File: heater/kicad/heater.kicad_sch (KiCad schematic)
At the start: 85 parts, among them J1 Conn_01x02_Pin, J2 Conn_01x02_Pin, J3 pcie_98, U1 OPA863SIDBVR, U11 ESD5344D-TP, U12 ESD5344D-TP, U13 XC6206P332MR, U15 TPS7A2025PDBVR, U2 D050505T-1WR4, U3 LTC1966, U5 TPS72325DBVR, U6 LTC1966, U8 ADS1115IDGS, U9 ISO1541

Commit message: Updated heater shecmatic and sys config.
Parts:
- R6: value 10K -> 1K; LCSC C25744 -> C11702
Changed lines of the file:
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@@
       (effects (font (size 1.27 1.27)))
     )
-    (property "Value" "10K" (at 138.43 123.19 90)
+    (property "Value" "1K" (at 138.43 123.19 90)
       (effects (font (size 1.27 1.27)))
     )
@@
       (effects (font (size 1.27 1.27)) hide)
     )
-    (property "LCSC" "C25744" (at 138.43 125.73 0)
+    (property "LCSC" "C11702" (at 138.43 125.73 0)
       (effects (font (size 1.27 1.27)) hide)
     )

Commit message: Changed value of isense op amp serial resistor.
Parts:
- R6: value 1K -> 910R; LCSC C11702 -> (none)
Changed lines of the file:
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@@
       (effects (font (size 1.27 1.27)))
     )
-    (property "Value" "1K" (at 138.43 123.19 90)
+    (property "Value" "910R" (at 138.43 123.19 90)
       (effects (font (size 1.27 1.27)))
     )
@@
       (effects (font (size 1.27 1.27)) hide)
     )
-    (property "LCSC" "C11702" (at 138.43 125.73 0)
+    (property "LCSC" "" (at 138.43 125.73 0)
       (effects (font (size 1.27 1.27)) hide)
     )

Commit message: Fixed the heater schematic title.
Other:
- title: ADS1261B ADC BOARD -> PWM Power Measurement Card.
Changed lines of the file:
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@@
   (paper "User" 381 279.4)
   (title_block
-    (title "ADS1261B ADC BOARD")
+    (title "PWM Power Measurement Card.")
     (rev "0.2")
   )

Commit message: Changed the I sense op amp to a low bias current one.
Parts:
- R6: value 910R -> 10K; LCSC (none) -> C25744
- U1: value OPA863SIDBVR -> OPA810IDBV; LCSC C4369756 -> C2833513
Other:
- note added: "NOTES: * LCSC part number are of approximated values to maximize usage of JLCPCB 'basic' parts. * Accuracy can be improved by suing low ppm resistors where applicable and a film capacitor for the RMS converter integrator. * JLCPCB fabrication files should be generated using the Kicad's Fabrication Toolkit plugin. * OPA810IDBVT was selected for high slew rate, low current offset, and low voltage o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"
- note removed: "NOTES: * LCSC part number are of approximated values to maximize usage of JLCPCB 'basic' parts. * Accuracy can be improved by suing low ppm resistors where applicable and a film capacitor for the RMS converter integrator. * JLCPCB fabrication files should be generated using the Kicad's Fabrication Toolkit plugin. * Substitute OPA863SIDBVR with OPA863DBVR. * Substitute ISO1541 with ISO1641BDR. * S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"
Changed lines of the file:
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@@
     (effects (font (size 1.27 1.27)) (justify left bottom))
   )
-  (text "NOTES: \n* LCSC part number are of approximated values to maximize usage of JLCPCB 'basic' parts.\n* Accuracy can be improved by suing low ppm resistors where applicable and a film \n  capacitor for the RMS converter integrator.\n* JLCPCB fabrication files should be generated using the Kicad's Fabrication Toolkit\n  plugin.\n* Substitute OPA863SIDBVR with OPA863DBVR.\n* Substitute ISO1541 with ISO1641BDR.\n* Substitute LTC1966 with LTC1967, LTC1968\n* Several 0R resistors where added to allow to disconnect for diagnostics.\n* The ground plane under the shunt resistor is isolated thermally from\n  the rest of the ground plane.\n"
+  (text "NOTES: \n* LCSC part number are of approximated values to maximize usage of JLCPCB 'basic' parts.\n* Accuracy can be improved by suing low ppm resistors where applicable and a film \n  capacitor for the RMS converter integrator.\n* JLCPCB fabrication files should be generated using the Kicad's Fabrication Toolkit\n  plugin.\n* OPA810IDBVT was selected for high slew rate, low current offset, \n  and low voltage offset. \n* Substitute ISO1541 with ISO1641BDR.\n* Substitute LTC1966 with LTC1967, LTC1968\n* Several 0R resistors where added to allow to disconnect for diagnostics.\n* The ground plane under the shunt resistor is isolated thermally from\n  the rest of the ground plane.\n"
     (at 251.46 227.33 0)
     (effects (font (size 1.27 1.27)) (justify left bottom))
@@
       (effects (font (size 1.27 1.27)))
     )
-    (property "Value" "OPA863SIDBVR" (at 139.7 139.7 0)
+    (property "Value" "OPA810IDBV" (at 139.7 139.7 0)
       (effects (font (size 1.27 1.27)))
     )
@@
       (effects (font (size 1.27 1.27)) hide)
     )
-    (property "LCSC" "C4369756" (at 152.4 128.27 0)
+    (property "LCSC" "C2833513" (at 152.4 128.27 0)
       (effects (font (size 1.27 1.27)) hide)
     )
@@
       (effects (font (size 1.27 1.27)))
     )
-    (property "Value" "910R" (at 138.43 123.19 90)
+    (property "Value" "10K" (at 138.43 123.19 90)
       (effects (font (size 1.27 1.27)))
     )
@@
       (effects (font (size 1.27 1.27)) hide)
     )
-    (property "LCSC" "" (at 138.43 125.73 0)
+    (property "LCSC" "C25744" (at 138.43 125.73 0)
       (effects (font (size 1.27 1.27)) hide)
     )

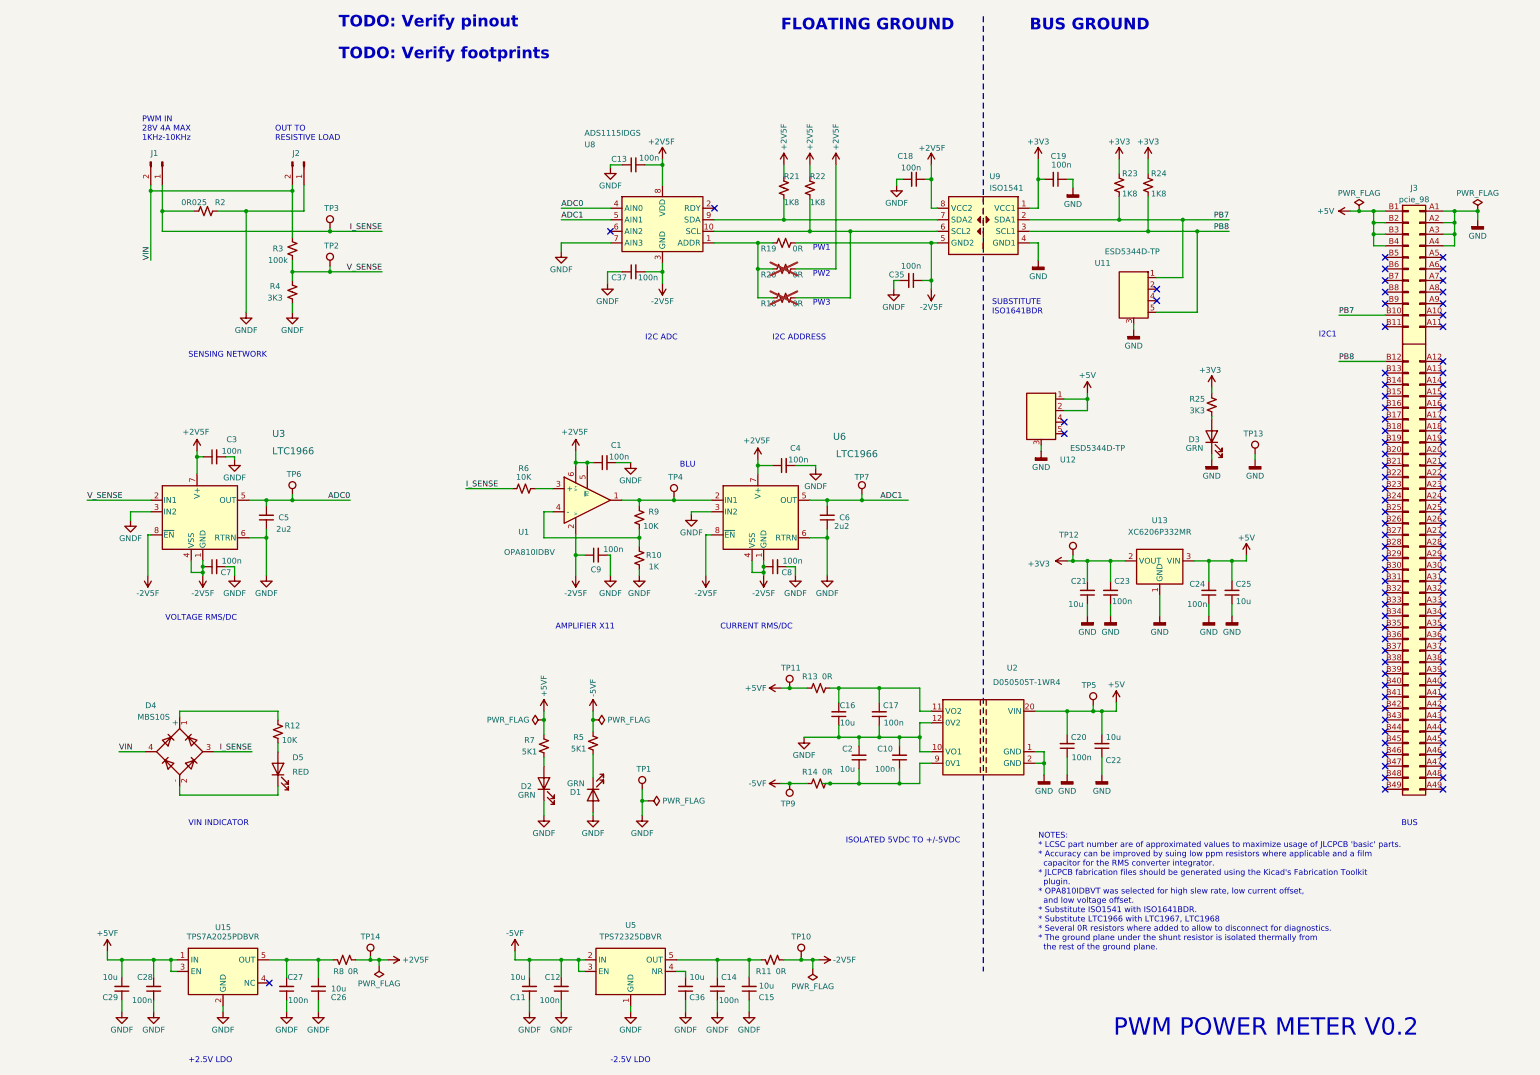
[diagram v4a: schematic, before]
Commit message: Added comments to the heater schematic.
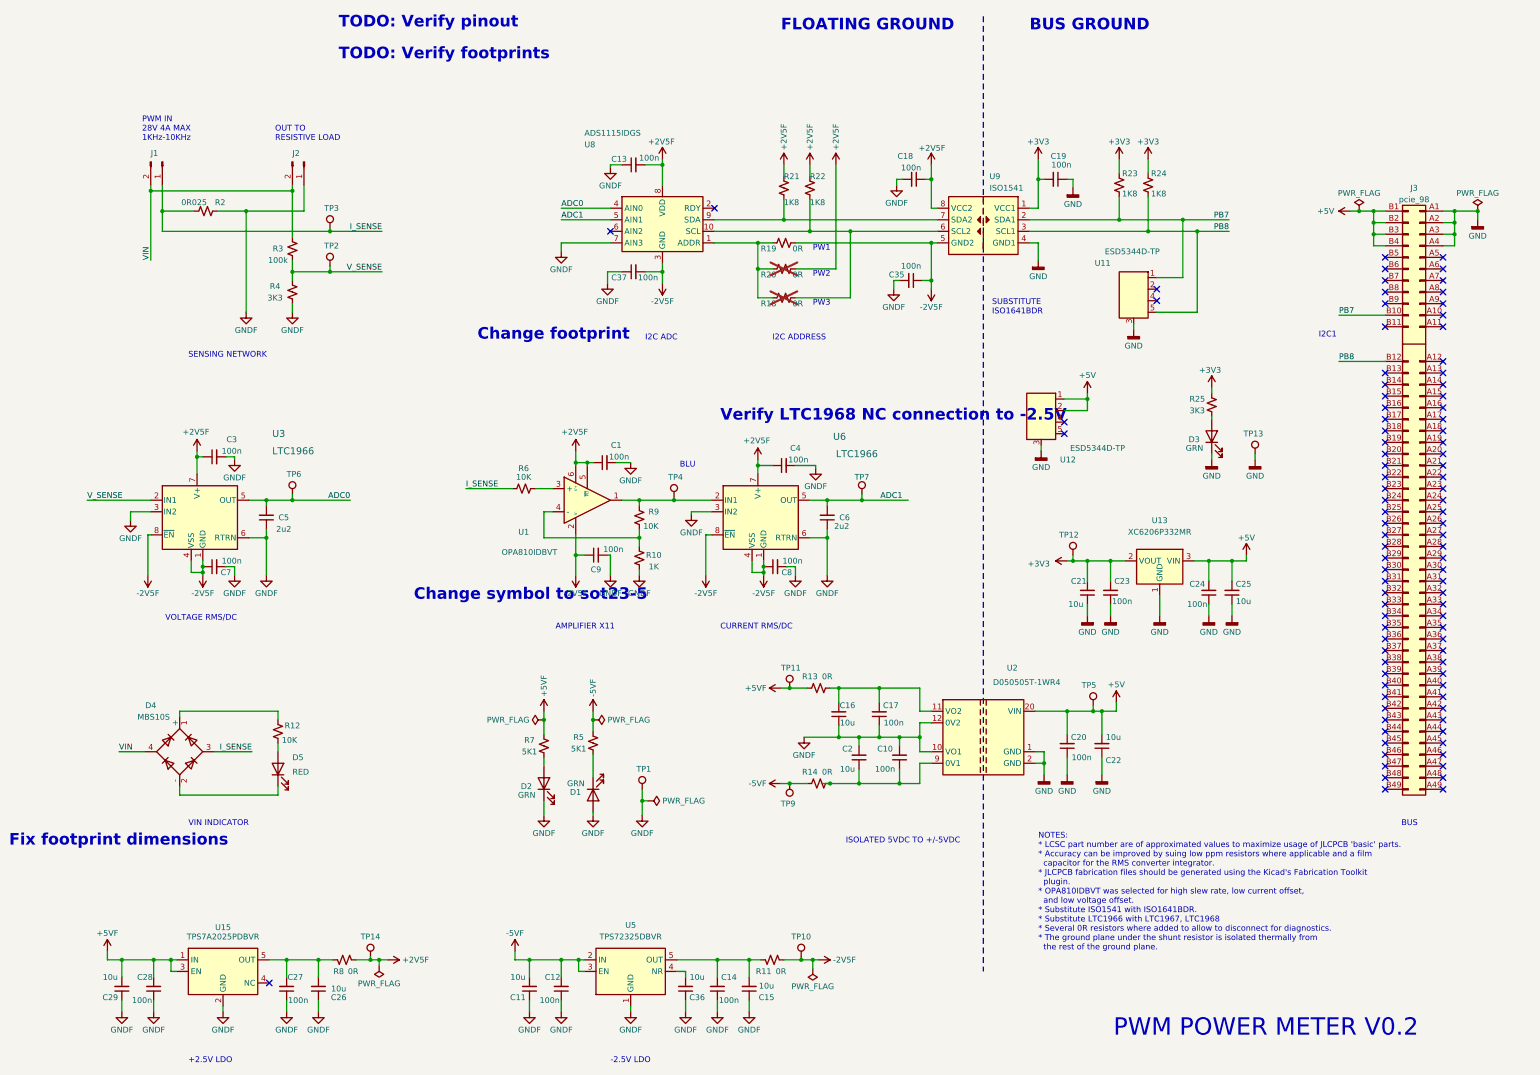
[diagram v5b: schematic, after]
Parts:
- U1: value OPA810IDBV -> OPA810IDBVT; LCSC C2833513 -> (none)
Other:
- note added: "Change footprint"
- note added: "Change symbol to sot23-5"
- note added: "Fix footprint dimensions"
- note added: "Verify LTC1968 NC connection to -2.5V"
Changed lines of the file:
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@@
     (effects (font (size 2.54 2.54) (thickness 0.508) bold (color 255 0 0 1)) (justify left bottom))
   )
+  (text "Verify LTC1968 NC connection to -2.5V" (at 181.61 111.125 0)
+    (effects (font (size 2.54 2.54) (thickness 0.508) bold (color 255 0 0 1)) (justify left bottom))
+  )
   (text "PW1" (at 201.93 73.66 0)
     (effects (font (size 1.27 1.27)) (justify left bottom))
   )
+  (text "Fix footprint dimensions" (at 25.4 204.47 0)
+    (effects (font (size 2.54 2.54) (thickness 0.508) bold (color 255 0 0 1)) (justify left bottom))
+  )
   (text "-2.5V LDO" (at 157.48 252.095 0)
     (effects (font (size 1.27 1.27)) (justify left bottom))
@@
   (text "BLU" (at 172.72 121.285 0)
     (effects (font (size 1.27 1.27)) (justify left bottom))
+  )
+  (text "Change symbol to sot23-5" (at 114.3 150.495 0)
+    (effects (font (size 2.54 2.54) (thickness 0.508) bold (color 255 0 0 1)) (justify left bottom))
   )
   (text "I2C1" (at 313.055 92.71 0)
@@
   )
   (text "TODO: Verify pinout" (at 97.79 24.765 0)
+    (effects (font (size 2.54 2.54) (thickness 0.508) bold (color 255 0 0 1)) (justify left bottom))
+  )
+  (text "Change footprint" (at 128.27 93.345 0)
     (effects (font (size 2.54 2.54) (thickness 0.508) bold (color 255 0 0 1)) (justify left bottom))
   )
@@
       (effects (font (size 1.27 1.27)))
     )
-    (property "Value" "OPA810IDBV" (at 139.7 139.7 0)
+    (property "Value" "OPA810IDBVT" (at 139.7 139.7 0)
       (effects (font (size 1.27 1.27)))
     )
@@
       (effects (font (size 1.27 1.27)) hide)
     )
-    (property "LCSC" "C2833513" (at 152.4 128.27 0)
-      (effects (font (size 1.27 1.27)) hide)
-    )
+    (property "LCSC" "" (at 152.4 128.27 0)
+      (effects (font (size 1.27 1.27)) hide)
+    )

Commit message: Verified footprints and pinouts. (Recovered from a bad merge)
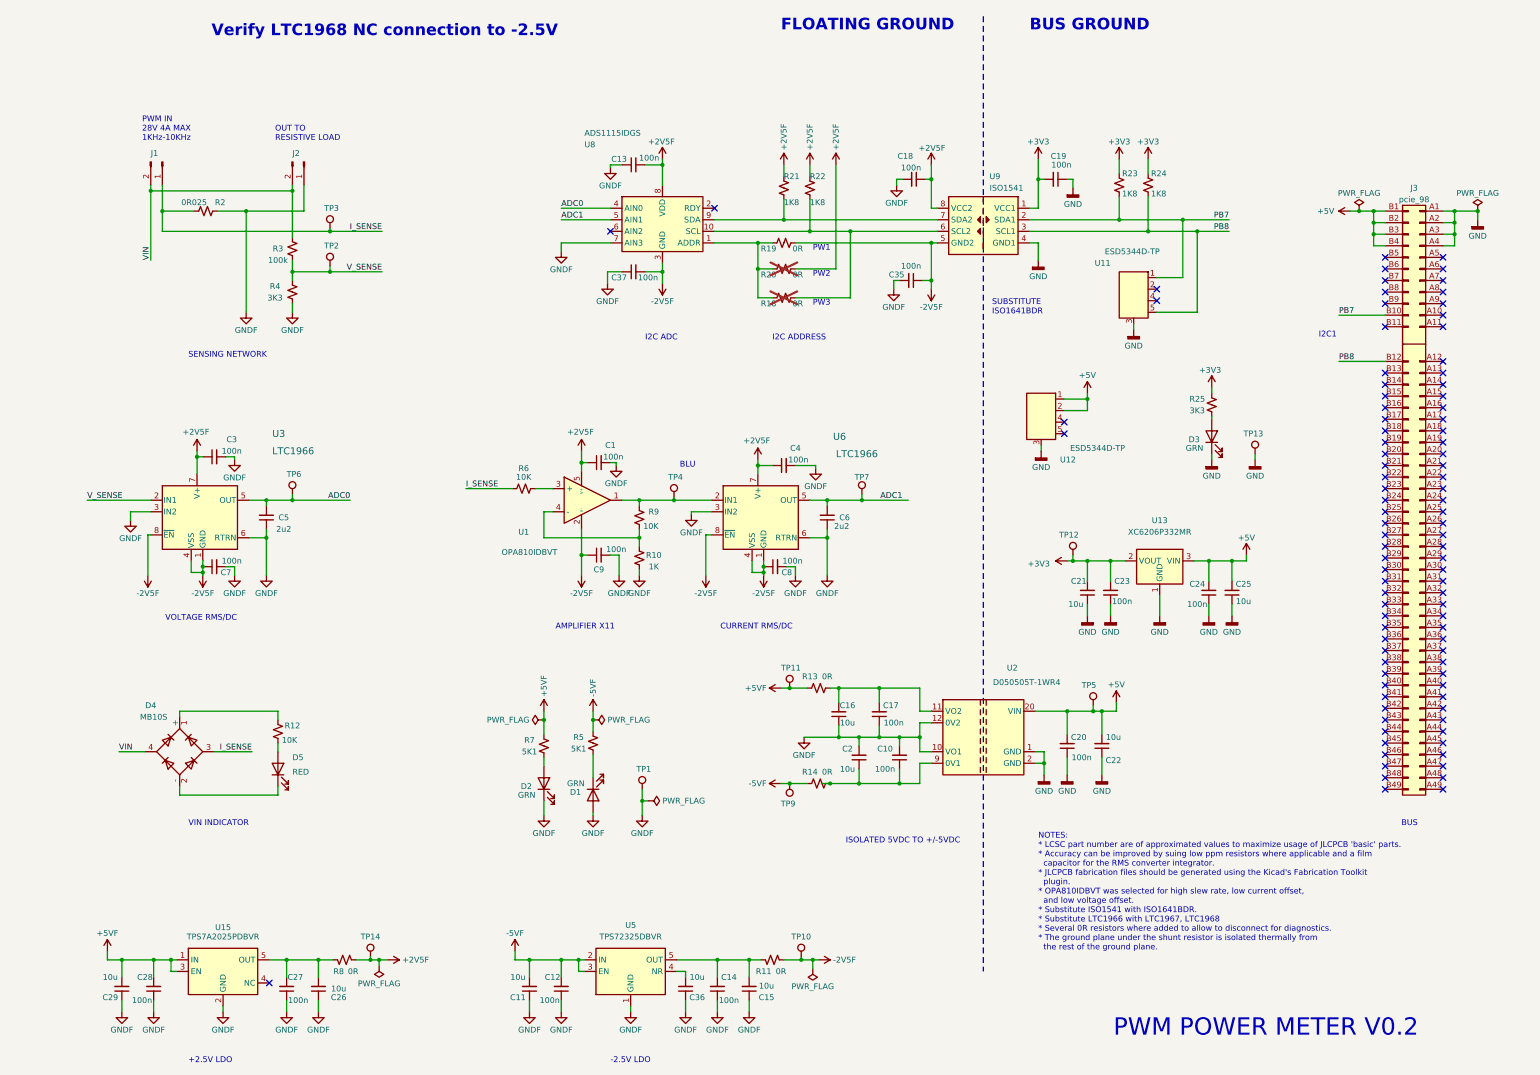
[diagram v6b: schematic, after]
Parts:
- D4: value MBS10S -> MB10S
- U1: footprint Package_TO_SOT_SMD:TSOT-23-6 -> Package_TO_SOT_SMD:TSOT-23-5; symbol heater:OPA863SIDBVR -> heater:OP_AMP_SOT-23-5
- U8: footprint Package_SO:TSSOP-10_3x3mm_P0.5mm -> Package_SO:VSSOP-10_3x3mm_P0.5mm
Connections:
- net +2V5F: no longer U1.6 (V+)
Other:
- note removed: "Change footprint"
- note removed: "Change symbol to sot23-5"
- note removed: "Fix footprint dimensions"
- note removed: "TODO: Verify footprints"
- note removed: "TODO: Verify pinout"
- moved on the sheet: C1, C9

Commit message: Added an indicator led for reversed VIN.
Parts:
- removed D4: MB10S, common:Diode_Bridge_MBS10, symbol Diode_Bridge:ABS10
- added D4: YEL, LED_SMD:LED_0603_1608Metric, symbol Device:LED
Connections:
- net I_SENSE: now also D5.1 (K), D4.2 (A)
- net VIN: now also R12.1
- net at D5.2 (A), R12.2: now also D4.1 (K)
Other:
- note added: "+"
- note added: "-"
- note added: "NEGATIVE"
- note added: "POSITIVE"
- note added: "VIN AND POLARITY INDICATOR"
- note removed: "VIN INDICATOR"
- note removed: "Verify LTC1968 NC connection to -2.5V"
- moved on the sheet: D5, R12

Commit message: Tweaked the vin indicator.
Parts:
- U1: LCSC (none) -> C4154868
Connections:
- net I_SENSE renamed -I_SENSE
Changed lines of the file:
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@@
     (effects (font (size 1.27 1.27)) (justify left bottom))
   )
-  (text "FLOATING GROUND" (at 194.945 25.4 0)
+  (text "FLOATING GROUND" (at 197.485 29.21 0)
     (effects (font (size 2.54 2.54) (thickness 0.508) bold) (justify left bottom))
   )
@@
   )
   (text "NOTES: \n* LCSC part number are of approximated values to maximize usage of JLCPCB 'basic' parts.\n* Accuracy can be improved by suing low ppm resistors where applicable and a film \n  capacitor for the RMS converter integrator.\n* JLCPCB fabrication files should be generated using the Kicad's Fabrication Toolkit\n  plugin.\n* OPA810IDBVT was selected for high slew rate, low current offset, \n  and low voltage offset. \n* Substitute ISO1541 with ISO1641BDR.\n* Substitute LTC1966 with LTC1967, LTC1968\n* Several 0R resistors where added to allow to disconnect for diagnostics.\n* The ground plane under the shunt resistor is isolated thermally from\n  the rest of the ground plane.\n* I sense and V sense are calibrated for positive polarity input. Negative\n  polarity may introduce a small offset but should be in range."
-    (at 251.46 227.33 0)
+    (at 249.555 231.14 0)
     (effects (font (size 1.27 1.27)) (justify left bottom))
   )
@@
     (effects (font (size 1.27 1.27)) (justify right bottom))
   )
-  (text "BUS GROUND" (at 249.555 25.4 0)
+  (text "BUS GROUND" (at 245.745 29.21 0)
     (effects (font (size 2.54 2.54) (thickness 0.508) bold) (justify left bottom))
   )
@@
     (effects (font (size 1.27 1.27)) (justify right bottom))
   )
-  (label "I_SENSE" (at 125.73 125.73 0) (fields_autoplaced)
+  (label "-I_SENSE" (at 125.73 125.73 0) (fields_autoplaced)
     (effects (font (size 1.27 1.27)) (justify left bottom))
   )
@@
     (effects (font (size 1.27 1.27)) (justify right bottom))
   )
-  (label "I_SENSE" (at 107.315 69.215 180) (fields_autoplaced)
+  (label "-I_SENSE" (at 107.315 69.215 180) (fields_autoplaced)
     (effects (font (size 1.27 1.27)) (justify right bottom))
   )
@@
     (effects (font (size 1.27 1.27)) (justify left bottom))
   )
-  (label "I_SENSE" (at 98.425 184.785 180) (fields_autoplaced)
+  (label "-I_SENSE" (at 98.425 184.785 180) (fields_autoplaced)
     (effects (font (size 1.27 1.27)) (justify right bottom))
   )
@@
       (effects (font (size 1.27 1.27)) hide)
     )
-    (property "LCSC" "" (at 152.4 128.27 0)
-      (effects (font (size 1.27 1.27)) hide)
-    )
+    (property "LCSC" "C4154868" (at 152.4 128.27 0)
+      (effects (font (size 1.27 1.27)) hide)
+    )
